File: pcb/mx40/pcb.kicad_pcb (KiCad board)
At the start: 2 copper layers, 321 x 92.3 mm, 181 parts, among them SW1 Switch, SW10 Switch, SW11 Switch, SW12 Switch, SW13 Switch, SW14 Switch, SW15 Switch, SW16 Switch, SW17 Switch, SW18 Switch, SW19 Switch, SW2 Switch, SW20 Switch, SW21 Switch, SW22 Switch, SW23 Switch, SW24 Switch, SW25 Switch, SW26 Switch, SW27 Switch, SW28 Switch, SW29 Switch, SW3 Switch, SW30 Switch, SW31 Switch, SW32 Switch, SW33 Switch, SW34 Switch, SW35 Switch, SW36 Switch, SW37 Switch, SW38 Switch, SW39 Switch, SW4 Switch, SW40 Switch, SW5 Switch, SW6 Switch, SW7 Switch, SW8 Switch, SW9 Switch

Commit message: small updates
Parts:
- moved H3 8.28 mm to (47.5, 72.0)
- moved H15 8.28 mm to (310.5, 72.0)
- moved H9 3.06 mm to (217.6, 127.1)
- moved H6 3.06 mm to (140.4, 127.1)
- moved H14 2.40 mm to (217.6, 68.5)
- moved H1 1.90 mm to (172.0, 127.1)
- moved H13 1.90 mm to (186.0, 127.1)
- moved H12 1.80 mm to (264.0, 127.5)
- moved H16 1.50 mm to (299.0, 127.0)
- moved H11 0.50 mm to (59.0, 127.0)
- moved H7 0.45 mm to (94.0, 127.5)
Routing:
- net GNDA: track 17.9 -> 56.3 mm, vias 6 -> 8
- net GND: track 1.95 -> 14.3 mm, vias 7 -> 8
- net +3.3V: track 105.6 -> 106.1 mm

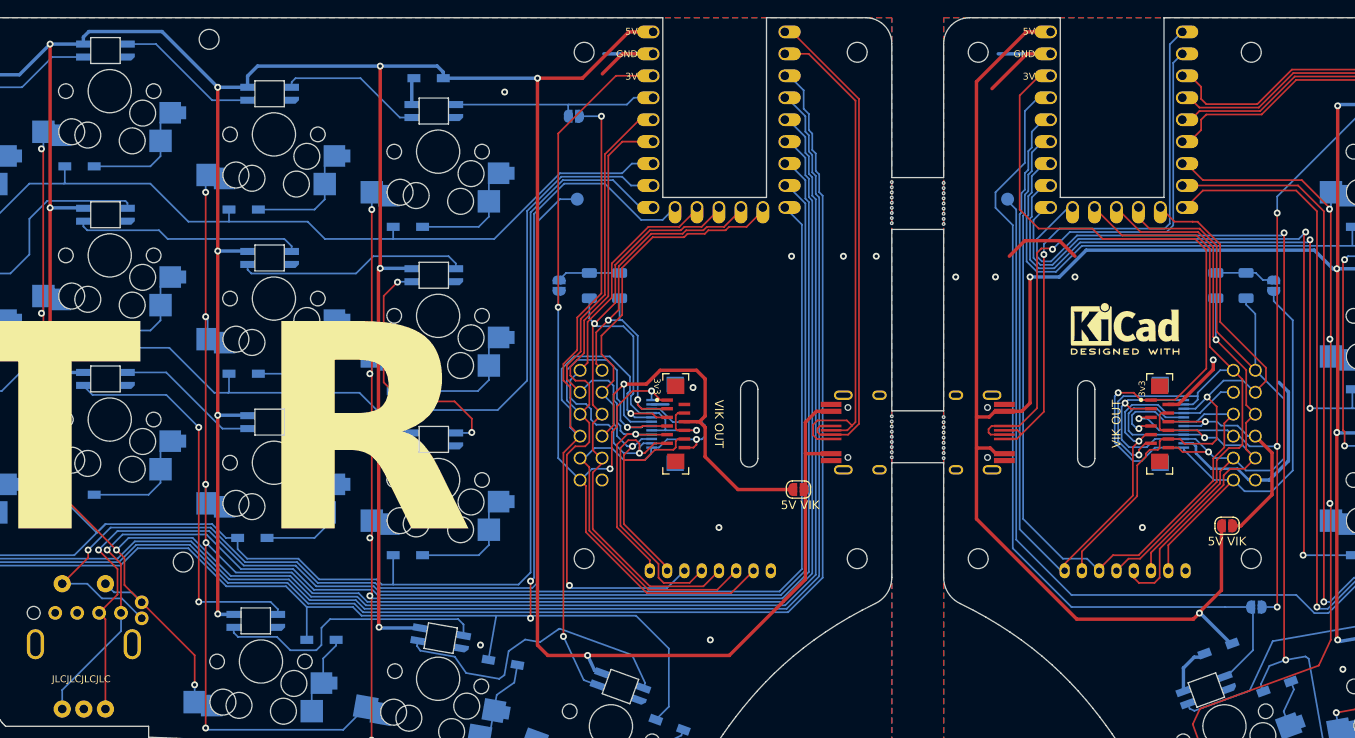
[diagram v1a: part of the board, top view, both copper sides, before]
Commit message: improve routing, rename case files
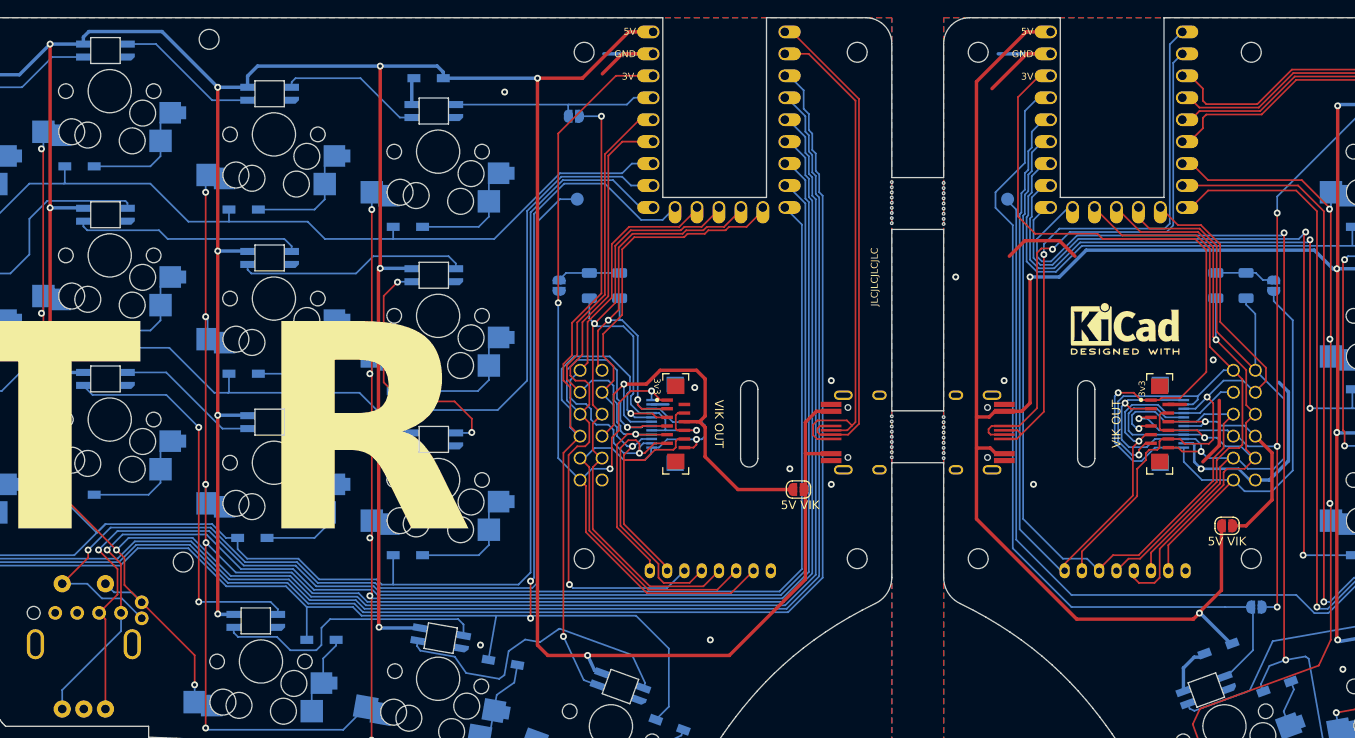
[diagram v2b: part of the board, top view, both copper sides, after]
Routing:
- net GNDA: track 56.3 -> 58.9 mm
- net +3.3VP: track 133.1 -> 134.9 mm
- net MISO: track 75.8 -> 77.1 mm
- net MOSI/SCL: track 99.1 -> 100.4 mm
- net SCLK/SDA: track 108.4 -> 109.5 mm
- net CS: track 71.9 -> 73.0 mm
- net CS_r: track 70.4 -> 69.8 mm
- net GND: vias 8 -> 7
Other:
- board text added: "MX40 v1.0"
- board text removed: "MX40 v0.1"

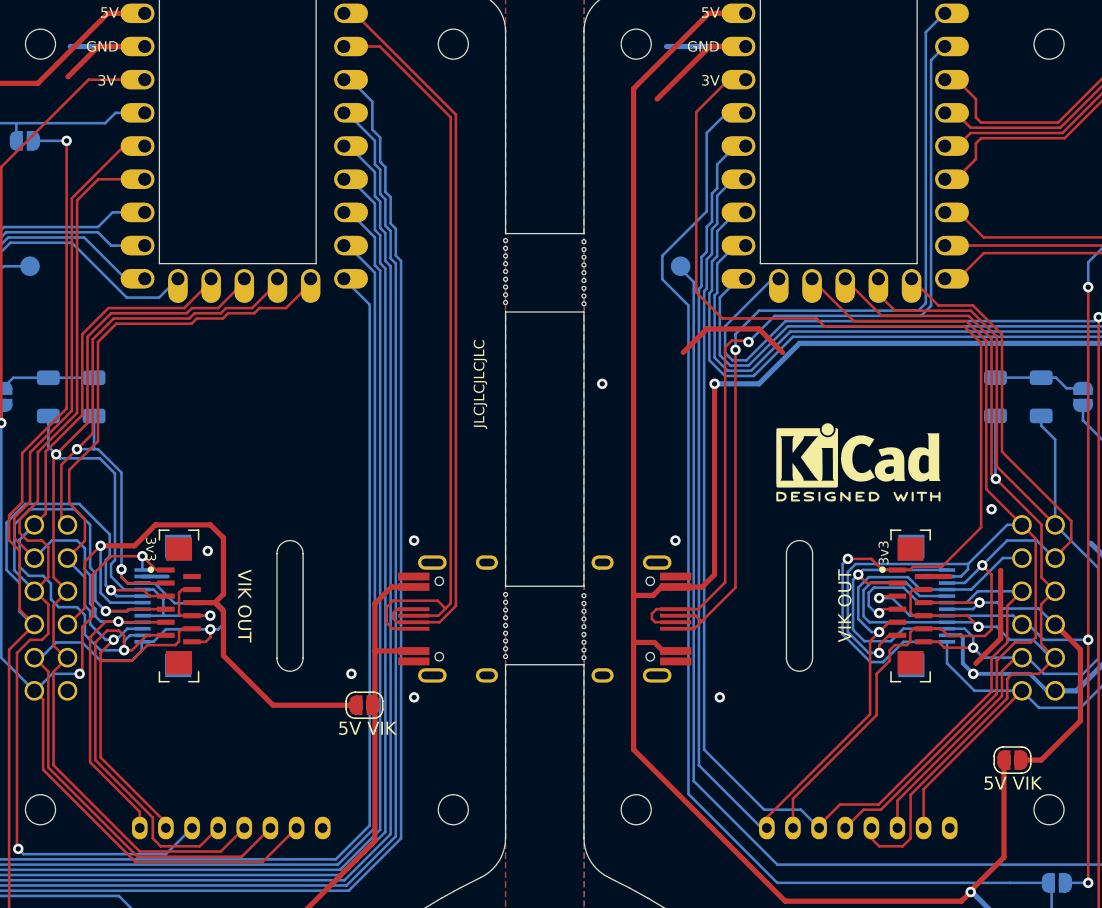
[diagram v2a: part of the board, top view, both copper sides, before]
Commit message: replace vertical VIK footprint for easier soldering
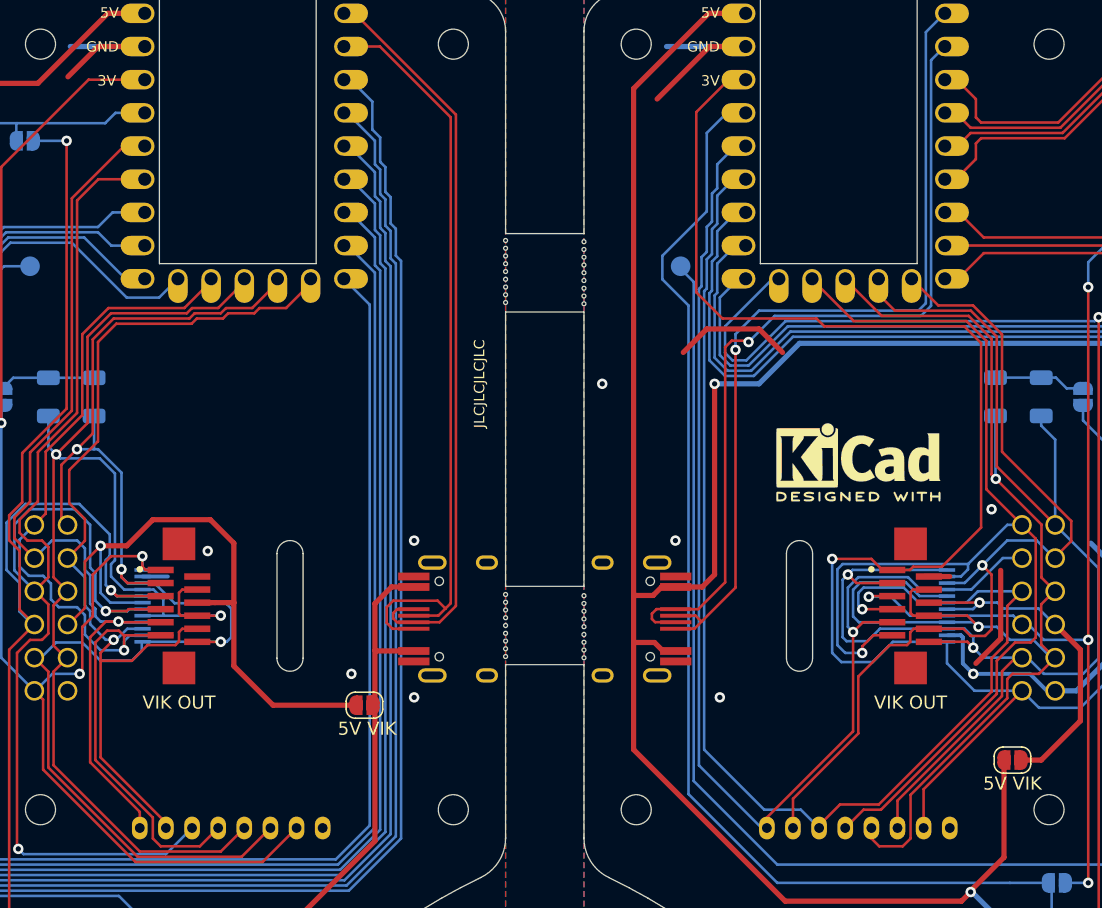
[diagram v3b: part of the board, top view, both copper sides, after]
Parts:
- VIK_K1, VIK_K4: footprint vik:vik-keyboard-connector-vertical -> zzkeeb:Connector_VIK-vertical-keyboard
- turned VIK_K1 to 0 degrees
- turned VIK_K4 to 0 degrees
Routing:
- net SCLK/SDA_r: track 105.7 -> 108.5 mm
- net +3.3VP: track 134.9 -> 137.6 mm
- net MISO_r: track 88.6 -> 90.9 mm
- net SCLK/SDA: track 109.5 -> 111.3 mm
- net MOSI/SCL_r: track 103.0 -> 104.6 mm
- net LED_OUT_r: track 82.7 -> 84.3 mm
- net MOSI/SCL: track 100.4 -> 102.0 mm
- net 5V_VIK: track 47.6 -> 49.1 mm
- net GPIO1_r: track 99.4 -> 100.7 mm
- net GPIO2_r: track 95.4 -> 96.5 mm
